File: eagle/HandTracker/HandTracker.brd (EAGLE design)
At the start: 53.3 x 50.5 mm, 29 parts, among them IC1 FT232RL, J1 ZX62-AB-5PA(31), U1 LSM9DS1TR, U2 MAX11629EEE+21-0055_E16+5_MXM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

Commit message: replaced rgb led with three LEDs
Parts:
- removed U$2: NTE30158, RGB LED:NTE30158
- added D1, D2, D3: SFH482, led:SFH482
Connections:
- net BLED_RES: now also D3.A; no longer U$2.P$1
- net GLED_RES: now also D2.A; no longer U$2.P$2
- net GND: now also D1.K, D2.K, D3.K; no longer U$2.P$3
- net RLED_RES: now also D1.A; no longer U$2.P$4
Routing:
- net RLED_RES: track 5.21 -> 2.79 mm
- net BLED_RES: track 4.98 -> 3.30 mm
- net GLED_RES: track 4.89 -> 3.83 mm
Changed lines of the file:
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@@
 <drawing>
 <settings>
-<setting alwaysvectorfont="yes"/>
+<setting alwaysvectorfont="no"/>
 <setting verticaltext="up"/>
 </settings>
@@
 <attribute name="VALUE" x="14.7151" y="24.7799" size="1.27" layer="27"/>
 </element>
-<element name="U$2" library="RGB LED" package="NTE30158" value="NTE30158" x="37.04" y="21.98" smashed="yes" rot="R90"/>
 <element name="U1" library="LSM9DS1" package="LGA-24_3X3P5X1_STM" value="LSM9DS1TR" x="6.41" y="37.1" smashed="yes" rot="R180">
 <attribute name="COPYRIGHT" value="Copyright (C) 2022 Ultra Librarian. All rights reserved." x="-50.74" y="114.57" size="1.778" layer="27" rot="R180" display="off"/>
@@
 <attribute name="NAME" x="38.2566" y="39.185" size="1.27" layer="27" ratio="6" rot="SR180"/>
 <attribute name="VALUE" x="36.7072" y="39.185" size="1.27" layer="21" ratio="6" rot="SR180"/>
+</element>
+<element name="D1" library="led" library_urn="urn:adsk.eagle:library:259" package="SFH482" package3d_urn="urn:adsk.eagle:package:15795/1" value="SFH482" x="-22.5" y="-12" smashed="yes">
+<attribute name="NAME" x="-23.77" y="-8.952" size="1.27" layer="25" ratio="10"/>
+<attribute name="POPULARITY" value="0" x="-22.5" y="-12" size="1.778" layer="27" display="off"/>
+<attribute name="VALUE" x="-23.77" y="-16.318" size="1.27" layer="27" ratio="10"/>
+</element>
+<element name="D2" library="led" library_urn="urn:adsk.eagle:library:259" package="SFH482" package3d_urn="urn:adsk.eagle:package:15795/1" value="SFH482" x="-31.5" y="-12" smashed="yes">
+<attribute name="NAME" x="-32.77" y="-8.952" size="1.27" layer="25" ratio="10"/>
+<attribute name="POPULARITY" value="0" x="-31.5" y="-12" size="1.778" layer="27" display="off"/>
+<attribute name="VALUE" x="-32.77" y="-16.318" size="1.27" layer="27" ratio="10"/>
+</element>
+<element name="D3" library="led" library_urn="urn:adsk.eagle:library:259" package="SFH482" package3d_urn="urn:adsk.eagle:package:15795/1" value="SFH482" x="-40.5" y="-12" smashed="yes">
+<attribute name="NAME" x="-41.77" y="-8.952" size="1.27" layer="25" ratio="10"/>
+<attribute name="POPULARITY" value="0" x="-40.5" y="-12" size="1.778" layer="27" display="off"/>
+<attribute name="VALUE" x="-41.77" y="-16.318" size="1.27" layer="27" ratio="10"/>
 </element>
 </elements>
@@
 <contactref element="IC1" pad="25"/>
 <contactref element="IC1" pad="26"/>
-<contactref element="U$2" pad="P$3"/>
 <contactref element="C9" pad="2"/>
 <contactref element="CR1" pad="7"/>
@@
 <wire x1="32.15425" y1="40.1375" x2="28.8625" y2="40.1375" width="0.254" layer="1"/>
 <wire x1="28.8625" y1="40.1375" x2="28.5" y2="40.5" width="0.254" layer="1"/>
+<contactref element="D1" pad="K"/>
+<contactref element="D2" pad="K"/>
+<contactref element="D3" pad="K"/>
+<wire x1="44.87" y1="40.48" x2="44.87" y2="45.56" width="0" layer="19" extent="1-1"/>
+<wire x1="44.87" y1="35.4" x2="44.87" y2="40.48" width="0" layer="19" extent="1-1"/>
+<wire x1="44.87" y1="30.32" x2="44.87" y2="35.4" width="0" layer="19" extent="1-1"/>
+<wire x1="44.87" y1="25.24" x2="44.87" y2="30.32" width="0" layer="19" extent="1-1"/>
+<wire x1="44.38" y1="19.72" x2="44.87" y2="25.24" width="0" layer="19" extent="1-1"/>
+<wire x1="49.28" y1="11.91" x2="44.38" y2="19.72" width="0" layer="19" extent="1-1"/>
+<wire x1="44.57" y1="8.92" x2="49.28" y2="11.91" width="0" layer="19" extent="1-1"/>
+<wire x1="49.32" y1="2" x2="44.57" y2="8.92" width="0" layer="19" extent="1-1"/>
+<wire x1="32.15425" y1="40.1375" x2="44.87" y2="40.48" width="0" layer="19" extent="1-1"/>
+<wire x1="18.84" y1="44.97" x2="28.5" y2="40.5" width="0" layer="19" extent="1-1"/>
+<wire x1="12.96" y1="44.99" x2="18.84" y2="44.97" width="0" layer="19" extent="1-1"/>
+<wire x1="9.46" y1="44.96" x2="12.96" y2="44.99" width="0" layer="19" extent="1-1"/>
+<wire x1="6.14" y1="44.85" x2="9.46" y2="44.96" width="0" layer="19" extent="1-1"/>
+<wire x1="4.959996875" y1="37.745" x2="6.14" y2="44.85" width="0" layer="19" extent="1-1"/>
+<wire x1="4.905" y1="35.9" x2="4.959996875" y2="36.455" width="0" layer="19" extent="1-1"/>
+<wire x1="5.335" y1="35.9" x2="4.905" y2="35.9" width="0" layer="19" extent="1-1"/>
+<wire x1="3.46" y1="29.31" x2="5.2983" y2="34.7983" width="0" layer="19" extent="1-1"/>
+<wire x1="7.46" y1="29.25" x2="3.46" y2="29.31" width="0" layer="19" extent="1-1"/>
+<wire x1="15.0651" y1="29.28" x2="7.46" y2="29.25" width="0" layer="19" extent="1-1"/>
+<wire x1="6.63" y1="19.96" x2="7.46" y2="29.25" width="0" layer="19" extent="1-1"/>
+<wire x1="4.3962" y1="12.505" x2="6.63" y2="19.96" width="0" layer="19" extent="1-1"/>
+<wire x1="8.16" y1="5.9619" x2="4.3962" y2="12.505" width="0" layer="19" extent="1-1"/>
+<wire x1="14.96" y1="4.11" x2="8.16" y2="5.9619" width="0" layer="19" extent="1-1"/>
+<wire x1="20.125" y1="3.435" x2="14.96" y2="4.11" width="0" layer="19" extent="1-1"/>
+<wire x1="20.125" y1="2.785" x2="20.125" y2="3.435" width="0" layer="19" extent="1-1"/>
+<wire x1="20.125" y1="6.035" x2="20.125" y2="3.435" width="0" layer="19" extent="1-1"/>
+<wire x1="20.125" y1="7.985" x2="20.125" y2="6.035" width="0" layer="19" extent="1-1"/>
+<wire x1="27.375" y1="5.385" x2="20.125" y2="6.035" width="0" layer="19" extent="1-1"/>
+<wire x1="-21.23" y1="-12" x2="2.5" y2="12.5" width="0" layer="19" extent="1-1"/>
+<wire x1="-30.23" y1="-12" x2="-21.23" y2="-12" width="0" layer="19" extent="1-1"/>
+<wire x1="-39.23" y1="-12" x2="-30.23" y2="-12" width="0" layer="19" extent="1-1"/>
 </signal>
 <signal name="VBUS">
@@
 </signal>
 <signal name="RLED_RES">
-<contactref element="U$2" pad="P$4"/>
 <contactref element="R9" pad="2"/>
 <wire x1="32.572" y1="27.58" x2="32.652" y2="27.5" width="0.254" layer="1"/>
-<wire x1="35.33" y1="27.5" x2="37.04" y2="25.79" width="0.254" layer="1"/>
 <wire x1="32.652" y1="27.5" x2="35.33" y2="27.5" width="0.254" layer="1"/>
+<contactref element="D1" pad="A"/>
+<wire x1="-23.77" y1="-12" x2="32.572" y2="27.58" width="0" layer="19" extent="1-1"/>
 </signal>
 <signal name="GLED_RES">
-<contactref element="U$2" pad="P$2"/>
 <contactref element="R10" pad="2"/>
 <wire x1="32.492" y1="24.08" x2="32.572" y2="24" width="0.254" layer="1"/>
-<wire x1="36.29" y1="24" x2="37.04" y2="23.25" width="0.254" layer="1"/>
 <wire x1="32.572" y1="24" x2="36.29" y2="24" width="0.254" layer="1"/>
+<contactref element="D2" pad="A"/>
+<wire x1="-32.77" y1="-12" x2="32.492" y2="24.08" width="0" layer="19" extent="1-1"/>
 </signal>
 <signal name="BLED_RES">
-<contactref element="U$2" pad="P$1"/>
 <contactref element="R11" pad="2"/>
 <wire x1="32.552" y1="20.79" x2="35.85" y2="20.79" width="0.254" layer="1"/>
-<wire x1="35.85" y1="20.79" x2="37.04" y2="21.98" width="0.254" layer="1"/>
+<contactref element="D3" pad="A"/>
+<wire x1="-41.77" y1="-12" x2="32.552" y2="20.79" width="0" layer="19" extent="1-1"/>
 </signal>
 </signals>

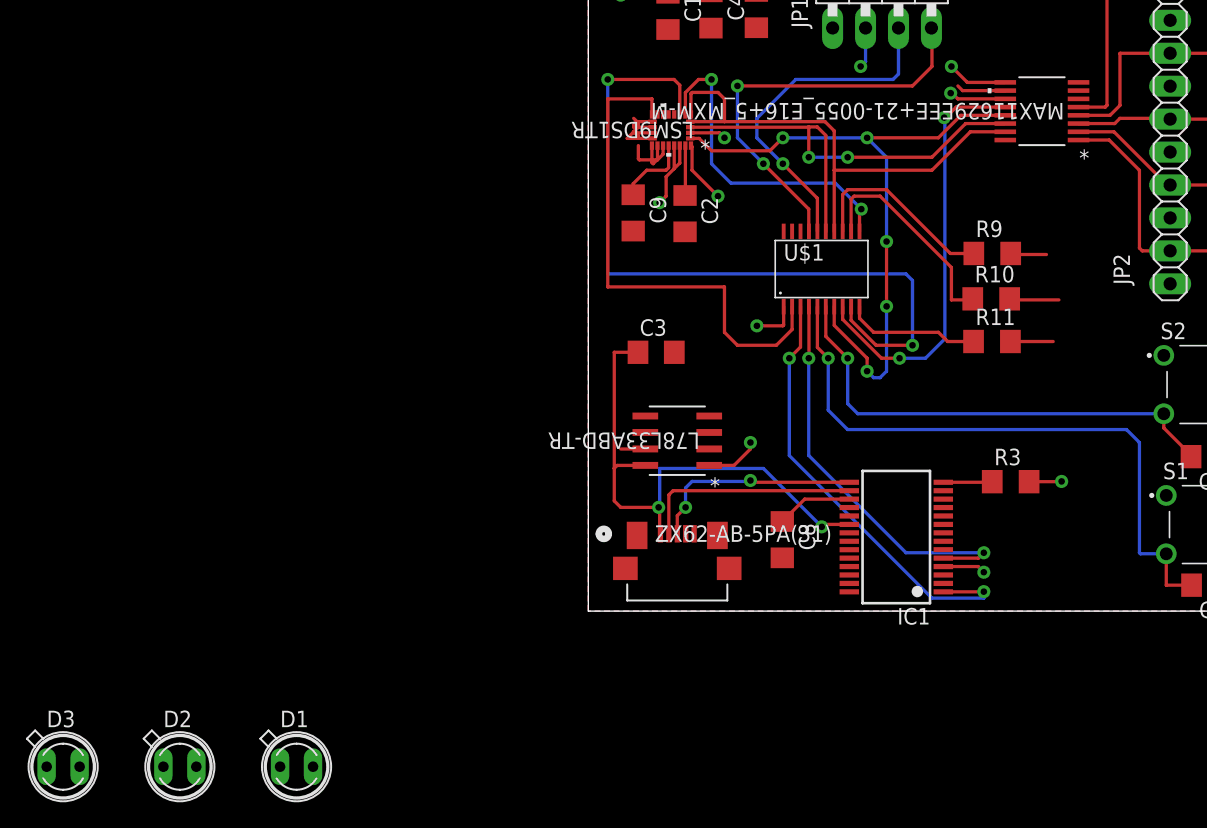
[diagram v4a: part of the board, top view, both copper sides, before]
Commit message: Routed LEDs and fixed clearance issues.
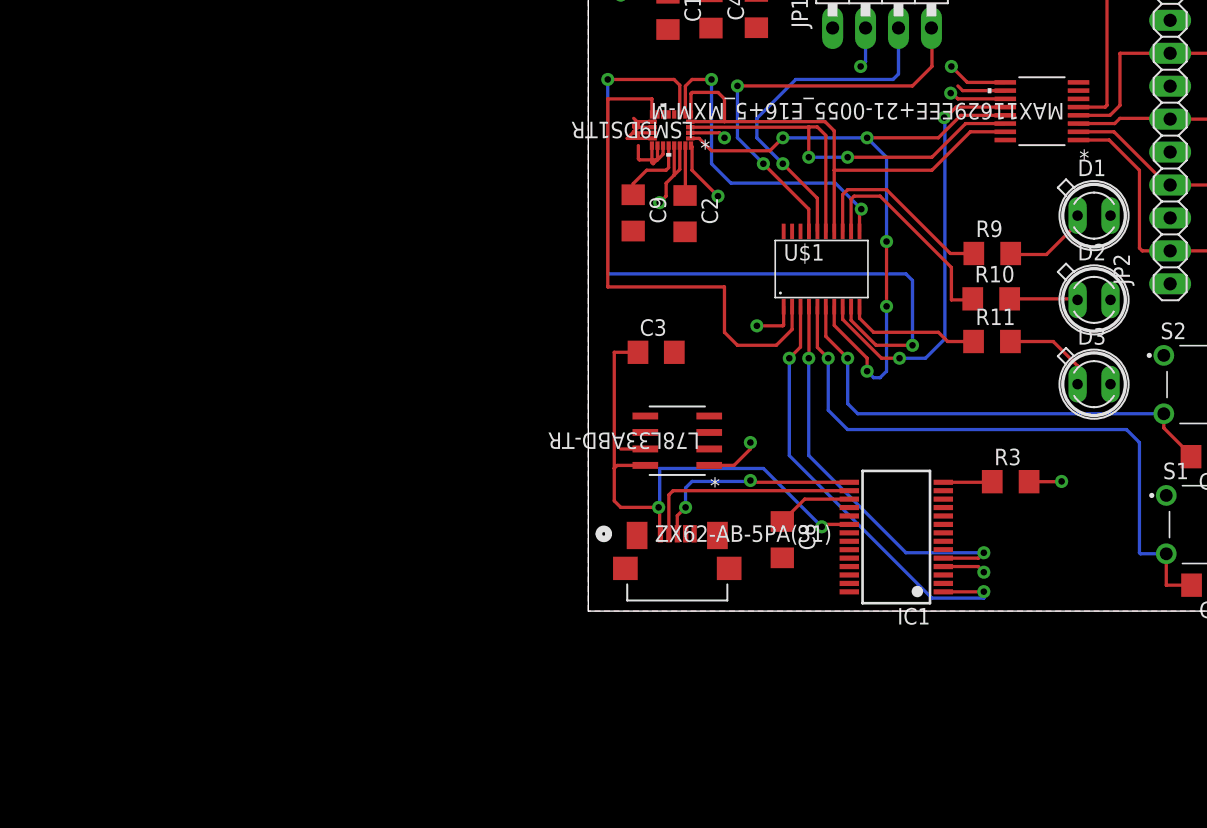
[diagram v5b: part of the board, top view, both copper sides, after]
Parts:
- moved D3 84.8 mm to (39.0, 17.5)
- moved D2 79.2 mm to (39.0, 24.0)
- moved D1 74.8 mm to (39.0, 30.5)
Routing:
- net BLED_RES: track 3.30 -> 7.37 mm
- net RLED_RES: track 2.79 -> 6.79 mm
- net GLED_RES: track 3.83 -> 5.38 mm
- net VCC: track 75.1 -> 75.6 mm
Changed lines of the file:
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@@
 <drawing>
 <settings>
-<setting alwaysvectorfont="no"/>
+<setting alwaysvectorfont="yes"/>
 <setting verticaltext="up"/>
 </settings>
@@
 <attribute name="VALUE" x="36.7072" y="39.185" size="1.27" layer="21" ratio="6" rot="SR180"/>
 </element>
-<element name="D1" library="led" library_urn="urn:adsk.eagle:library:259" package="SFH482" package3d_urn="urn:adsk.eagle:package:15795/1" value="SFH482" x="-22.5" y="-12" smashed="yes">
-<attribute name="NAME" x="-23.77" y="-8.952" size="1.27" layer="25" ratio="10"/>
-<attribute name="POPULARITY" value="0" x="-22.5" y="-12" size="1.778" layer="27" display="off"/>
-<attribute name="VALUE" x="-23.77" y="-16.318" size="1.27" layer="27" ratio="10"/>
-</element>
-<element name="D2" library="led" library_urn="urn:adsk.eagle:library:259" package="SFH482" package3d_urn="urn:adsk.eagle:package:15795/1" value="SFH482" x="-31.5" y="-12" smashed="yes">
-<attribute name="NAME" x="-32.77" y="-8.952" size="1.27" layer="25" ratio="10"/>
-<attribute name="POPULARITY" value="0" x="-31.5" y="-12" size="1.778" layer="27" display="off"/>
-<attribute name="VALUE" x="-32.77" y="-16.318" size="1.27" layer="27" ratio="10"/>
-</element>
-<element name="D3" library="led" library_urn="urn:adsk.eagle:library:259" package="SFH482" package3d_urn="urn:adsk.eagle:package:15795/1" value="SFH482" x="-40.5" y="-12" smashed="yes">
-<attribute name="NAME" x="-41.77" y="-8.952" size="1.27" layer="25" ratio="10"/>
-<attribute name="POPULARITY" value="0" x="-40.5" y="-12" size="1.778" layer="27" display="off"/>
-<attribute name="VALUE" x="-41.77" y="-16.318" size="1.27" layer="27" ratio="10"/>
+<element name="D1" library="led" library_urn="urn:adsk.eagle:library:259" package="SFH482" package3d_urn="urn:adsk.eagle:package:15795/1" value="SFH482" x="39" y="30.5" smashed="yes">
+<attribute name="NAME" x="37.73" y="33.548" size="1.27" layer="25" ratio="10"/>
+<attribute name="POPULARITY" value="0" x="39" y="30.5" size="1.778" layer="27" display="off"/>
+<attribute name="VALUE" x="37.73" y="26.182" size="1.27" layer="27" ratio="10"/>
+</element>
+<element name="D2" library="led" library_urn="urn:adsk.eagle:library:259" package="SFH482" package3d_urn="urn:adsk.eagle:package:15795/1" value="SFH482" x="39" y="24" smashed="yes">
+<attribute name="NAME" x="37.73" y="27.048" size="1.27" layer="25" ratio="10"/>
+<attribute name="POPULARITY" value="0" x="39" y="24" size="1.778" layer="27" display="off"/>
+<attribute name="VALUE" x="37.73" y="19.682" size="1.27" layer="27" ratio="10"/>
+</element>
+<element name="D3" library="led" library_urn="urn:adsk.eagle:library:259" package="SFH482" package3d_urn="urn:adsk.eagle:package:15795/1" value="SFH482" x="39" y="17.5" smashed="yes">
+<attribute name="NAME" x="37.73" y="20.548" size="1.27" layer="25" ratio="10"/>
+<attribute name="POPULARITY" value="0" x="39" y="17.5" size="1.778" layer="27" display="off"/>
+<attribute name="VALUE" x="37.73" y="13.182" size="1.27" layer="27" ratio="10"/>
 </element>
 </elements>
@@
 <contactref element="D2" pad="K"/>
 <contactref element="D3" pad="K"/>
-<wire x1="44.87" y1="40.48" x2="44.87" y2="45.56" width="0" layer="19" extent="1-1"/>
-<wire x1="44.87" y1="35.4" x2="44.87" y2="40.48" width="0" layer="19" extent="1-1"/>
-<wire x1="44.87" y1="30.32" x2="44.87" y2="35.4" width="0" layer="19" extent="1-1"/>
-<wire x1="44.87" y1="25.24" x2="44.87" y2="30.32" width="0" layer="19" extent="1-1"/>
-<wire x1="44.38" y1="19.72" x2="44.87" y2="25.24" width="0" layer="19" extent="1-1"/>
-<wire x1="49.28" y1="11.91" x2="44.38" y2="19.72" width="0" layer="19" extent="1-1"/>
-<wire x1="44.57" y1="8.92" x2="49.28" y2="11.91" width="0" layer="19" extent="1-1"/>
-<wire x1="49.32" y1="2" x2="44.57" y2="8.92" width="0" layer="19" extent="1-1"/>
-<wire x1="32.15425" y1="40.1375" x2="44.87" y2="40.48" width="0" layer="19" extent="1-1"/>
-<wire x1="18.84" y1="44.97" x2="28.5" y2="40.5" width="0" layer="19" extent="1-1"/>
-<wire x1="12.96" y1="44.99" x2="18.84" y2="44.97" width="0" layer="19" extent="1-1"/>
-<wire x1="9.46" y1="44.96" x2="12.96" y2="44.99" width="0" layer="19" extent="1-1"/>
-<wire x1="6.14" y1="44.85" x2="9.46" y2="44.96" width="0" layer="19" extent="1-1"/>
-<wire x1="4.959996875" y1="37.745" x2="6.14" y2="44.85" width="0" layer="19" extent="1-1"/>
-<wire x1="4.905" y1="35.9" x2="4.959996875" y2="36.455" width="0" layer="19" extent="1-1"/>
-<wire x1="5.335" y1="35.9" x2="4.905" y2="35.9" width="0" layer="19" extent="1-1"/>
-<wire x1="3.46" y1="29.31" x2="5.2983" y2="34.7983" width="0" layer="19" extent="1-1"/>
-<wire x1="7.46" y1="29.25" x2="3.46" y2="29.31" width="0" layer="19" extent="1-1"/>
-<wire x1="15.0651" y1="29.28" x2="7.46" y2="29.25" width="0" layer="19" extent="1-1"/>
-<wire x1="6.63" y1="19.96" x2="7.46" y2="29.25" width="0" layer="19" extent="1-1"/>
-<wire x1="4.3962" y1="12.505" x2="6.63" y2="19.96" width="0" layer="19" extent="1-1"/>
-<wire x1="8.16" y1="5.9619" x2="4.3962" y2="12.505" width="0" layer="19" extent="1-1"/>
-<wire x1="14.96" y1="4.11" x2="8.16" y2="5.9619" width="0" layer="19" extent="1-1"/>
-<wire x1="20.125" y1="3.435" x2="14.96" y2="4.11" width="0" layer="19" extent="1-1"/>
-<wire x1="20.125" y1="2.785" x2="20.125" y2="3.435" width="0" layer="19" extent="1-1"/>
-<wire x1="20.125" y1="6.035" x2="20.125" y2="3.435" width="0" layer="19" extent="1-1"/>
-<wire x1="20.125" y1="7.985" x2="20.125" y2="6.035" width="0" layer="19" extent="1-1"/>
-<wire x1="27.375" y1="5.385" x2="20.125" y2="6.035" width="0" layer="19" extent="1-1"/>
-<wire x1="-21.23" y1="-12" x2="2.5" y2="12.5" width="0" layer="19" extent="1-1"/>
-<wire x1="-30.23" y1="-12" x2="-21.23" y2="-12" width="0" layer="19" extent="1-1"/>
-<wire x1="-39.23" y1="-12" x2="-30.23" y2="-12" width="0" layer="19" extent="1-1"/>
 </signal>
 <signal name="VBUS">
@@
 <wire x1="12.5" y1="12.5" x2="12.5" y2="13" width="0.254" layer="1"/>
 <wire x1="11.235" y1="11.235" x2="12.5" y2="12.5" width="0.254" layer="1"/>
-<wire x1="6.625" y1="35.9" x2="6.625" y2="34.125" width="0.254" layer="1"/>
-<wire x1="6.625" y1="34.125" x2="6" y2="33.5" width="0.254" layer="1"/>
-<wire x1="6" y1="33.5" x2="6" y2="32" width="0.254" layer="1"/>
+<wire x1="6.625" y1="35.9" x2="6.625" y2="33.625" width="0.254" layer="1"/>
+<wire x1="6.625" y1="33.625" x2="6" y2="33" width="0.254" layer="1"/>
+<wire x1="6" y1="33" x2="6" y2="32" width="0.254" layer="1"/>
 <wire x1="5.5" y1="31.5" x2="6" y2="32" width="0.254" layer="1"/>
 <via x="5.5" y="31.5" extent="1-16" drill="0.508"/>
-<wire x1="7.055" y1="35.9" x2="7.055" y2="34.555" width="0.254" layer="1"/>
-<wire x1="7.055" y1="34.555" x2="6.625" y2="34.125" width="0.254" layer="1"/>
+<wire x1="7.055" y1="35.9" x2="7.055" y2="34.055" width="0.254" layer="1"/>
+<wire x1="7.055" y1="34.055" x2="6.625" y2="33.625" width="0.254" layer="1"/>
 <wire x1="7.860003125" y1="36.885" x2="10.115" y2="36.885" width="0.254" layer="1"/>
 <wire x1="10.115" y1="36.885" x2="10.5" y2="36.5" width="0.254" layer="1"/>
@@
 <wire x1="9.5" y1="34.5" x2="9.5" y2="41" width="0.254" layer="16"/>
 <via x="9.5" y="41" extent="1-16" drill="0.508"/>
-<wire x1="9.5" y1="41" x2="8.5" y2="41" width="0.254" layer="1"/>
-<wire x1="7.485" y1="39.985" x2="8.5" y2="41" width="0.254" layer="1"/>
-<wire x1="7.485" y1="38.3" x2="7.485" y2="39.985" width="0.254" layer="1"/>
+<wire x1="9.5" y1="41" x2="8" y2="41" width="0.254" layer="1"/>
+<wire x1="7.485" y1="40.485" x2="8" y2="41" width="0.254" layer="1"/>
+<wire x1="7.485" y1="38.3" x2="7.485" y2="40.485" width="0.254" layer="1"/>
 </signal>
 <signal name="CSM">
@@
 <wire x1="32.652" y1="27.5" x2="35.33" y2="27.5" width="0.254" layer="1"/>
 <contactref element="D1" pad="A"/>
-<wire x1="-23.77" y1="-12" x2="32.572" y2="27.58" width="0" layer="19" extent="1-1"/>
+<wire x1="35.33" y1="27.5" x2="37.73" y2="29.9" width="0.254" layer="1"/>
+<wire x1="37.73" y1="29.9" x2="37.73" y2="30.5" width="0.254" layer="1"/>
 </signal>
 <signal name="GLED_RES">
 <contactref element="R10" pad="2"/>
 <wire x1="32.492" y1="24.08" x2="32.572" y2="24" width="0.254" layer="1"/>
-<wire x1="32.572" y1="24" x2="36.29" y2="24" width="0.254" layer="1"/>
 <contactref element="D2" pad="A"/>
-<wire x1="-32.77" y1="-12" x2="32.492" y2="24.08" width="0" layer="19" extent="1-1"/>
+<wire x1="32.492" y1="24.08" x2="37.65" y2="24.08" width="0.254" layer="1"/>
+<wire x1="37.65" y1="24.08" x2="37.73" y2="24" width="0.254" layer="1"/>
 </signal>
 <signal name="BLED_RES">
@@
 <wire x1="32.552" y1="20.79" x2="35.85" y2="20.79" width="0.254" layer="1"/>
 <contactref element="D3" pad="A"/>
-<wire x1="-41.77" y1="-12" x2="32.552" y2="20.79" width="0" layer="19" extent="1-1"/>
+<wire x1="35.85" y1="20.79" x2="37.73" y2="18.91" width="0.254" layer="1"/>
+<wire x1="37.73" y1="18.91" x2="37.73" y2="17.5" width="0.254" layer="1"/>
 </signal>
 </signals>
